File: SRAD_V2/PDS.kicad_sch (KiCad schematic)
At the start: 16 parts, among them IC7 TPS563200, J5 Conn_01x02_Pin

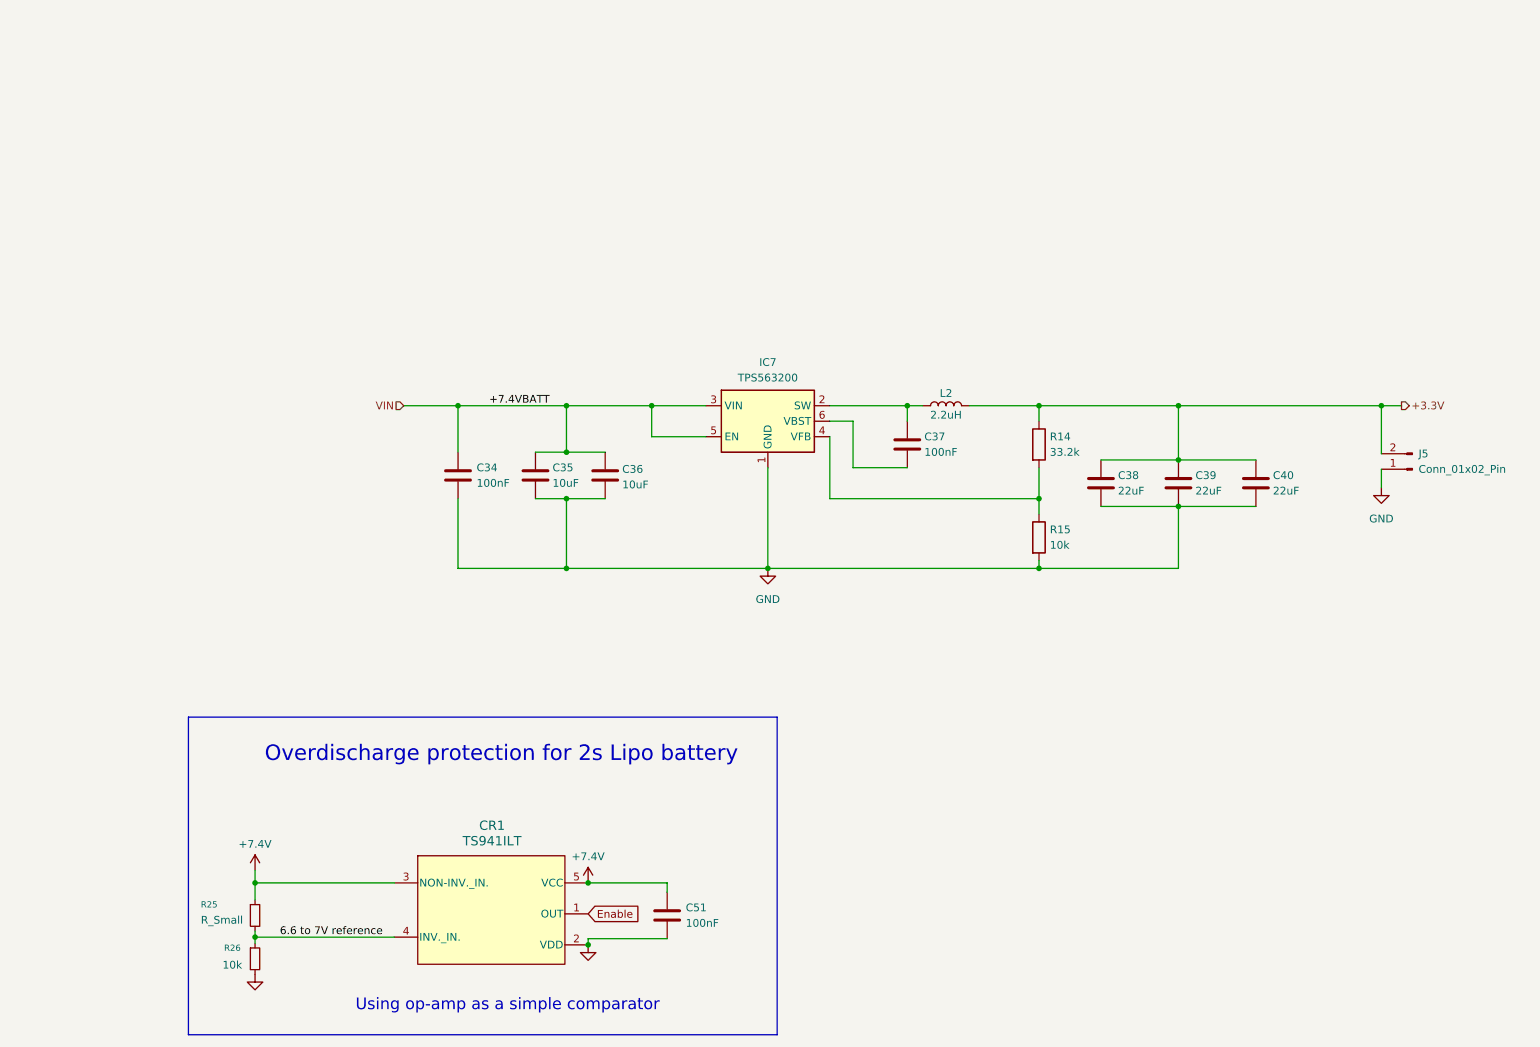
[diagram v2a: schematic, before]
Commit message: Added component descriptions for BOM and added logos on silkscreen
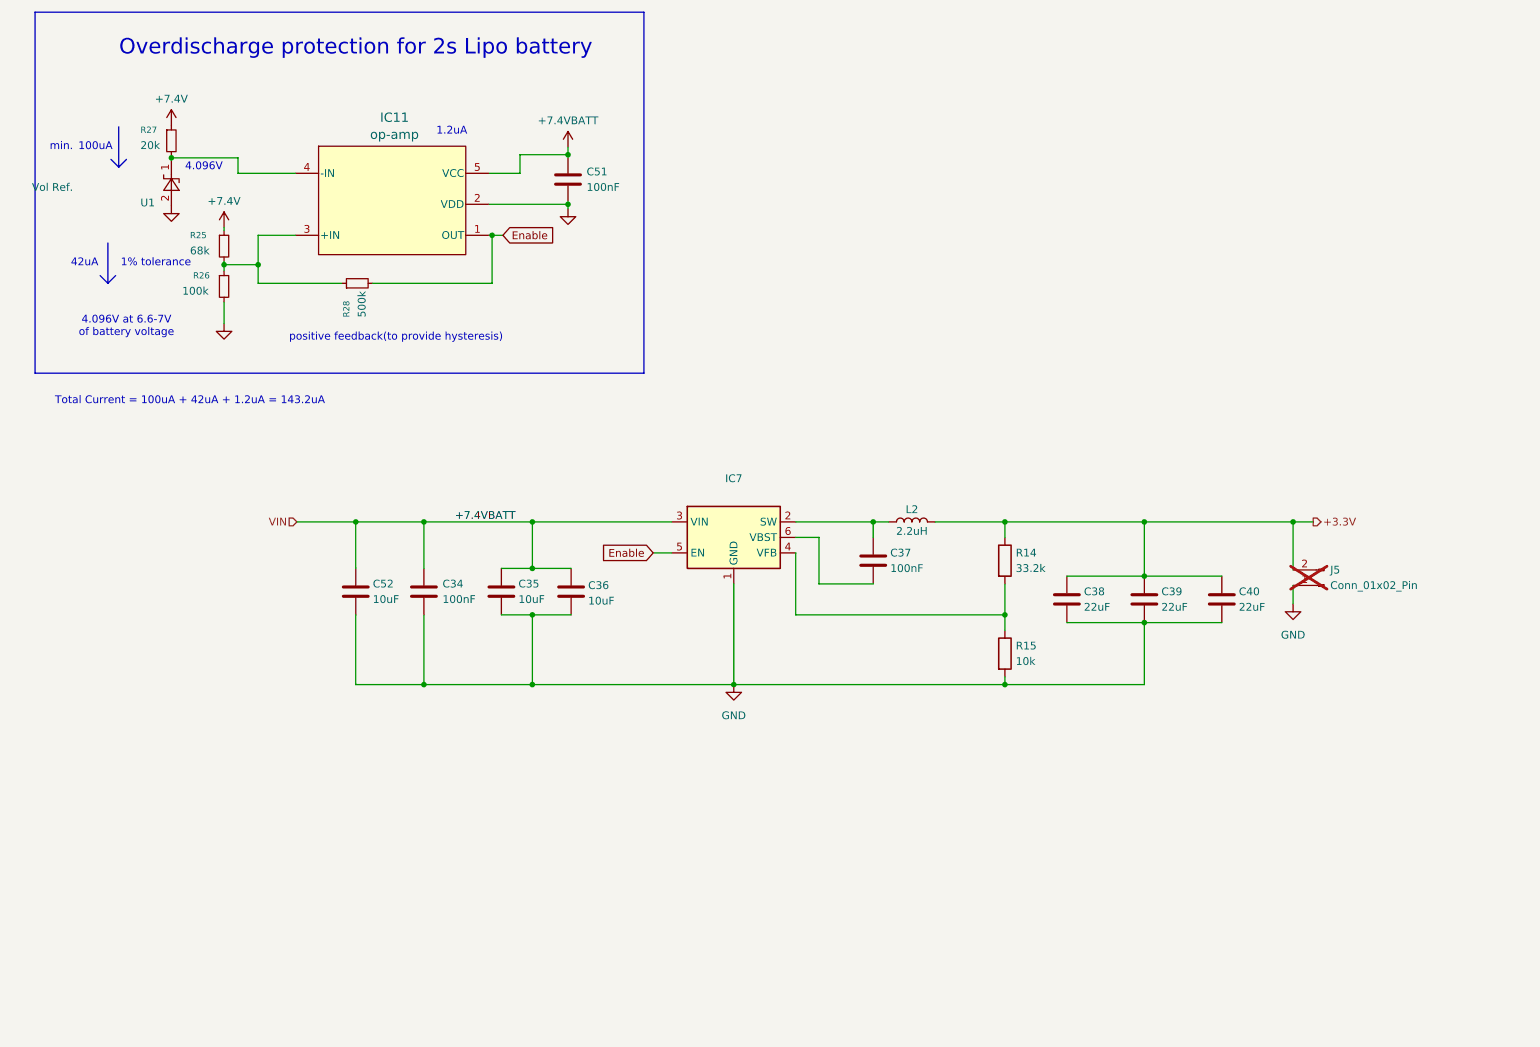
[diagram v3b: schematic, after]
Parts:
- added C52: 10uF, Capacitor_SMD:C_1206_3216Metric, symbol Device:C
- added R27: 20k, Resistor_SMD:R_0603_1608Metric, symbol Device:R_Small
- added R28: 500k, Resistor_SMD:R_0603_1608Metric, symbol Device:R_Small
- added U1: Vol Ref., Package_TO_SOT_SMD:SOT-23, symbol Reference_Voltage:LM4040DBZ-2.0
- C34, C37, C51: Digikey Link (none) -> https://www.digikey.ca/en/products/detail/kemet/C0603C104K5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; Manufacturer_Name (none) -> KEMET; Manufacturer_Part_Number (none) -> C0603C104K5RAC3121
- C35, C36: Digikey Link (none) -> https://www.digikey.com/en/products/detail/tdk/CGA5L1X7R1E1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; Manufacturer_Name (none) -> TDK; Manufacturer_Part_Number (none) -> CGA5L1X7R1E106K160DC
- C38, C39, C40: Digikey Link (none) -> https://www.digikey.com/en/products/detail/murata-electroni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; Manufacturer_Name (none) -> Murata Electronics; Manufacturer_Part_Number (none) -> GRM31CC81E226ME11L
- IC11: renamed from CR1; value TS941ILT -> op-amp; footprint TS941ILT:SOT23-5L_STM -> SOT23-5L_STM; Digikey Link (none) -> https://www.digikey.ca/en/products/detail/stmicroelectronic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; Manufacturer_Name (none) -> STMicroelectronics; Manufacturer_Part_Number (none) -> TS941ILT
- IC7: value TPS563200 -> (none); Digikey Link (none) -> https://www.digikey.ca/en/products/detail/texas-instruments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; Manufacturer_Name (none) -> Texas Instruments; Manufacturer_Part_Number (none) -> TPS563200DDCT
- J5: now not fitted
- L2: Digikey Link (none) -> https://www.digikey.ca/en/products/detail/bourns-inc/srp503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; Manufacturer_Name (none) -> Bourns Inc.; Manufacturer_Part_Number (none) -> SRP5030TA-2R2M
- R14: Digikey Link (none) -> https://www.digikey.ca/en/products/detail/vishay-dale/crcw0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; Manufacturer_Name (none) -> Vishay Dale; Manufacturer_Part_Number (none) -> CRCW060333K2FKTA
- R15: Digikey Link (none) -> https://www.digikey.ca/en/products/detail/bourns-inc/crt060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; Manufacturer_Name (none) -> Bourns Inc.; Manufacturer_Part_Number (none) -> CRT0603-BY-1002ELF
- R25: value R_Small -> 68k; Digikey Link (none) -> https://www.digikey.ca/en/products/detail/te-connectivity-p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; Manufacturer_Name (none) -> TE Connectivity Passive Product; Manufacturer_Part_Number (none) -> CRG0603F68K
- R26: value 10k -> 100k; Digikey Link (none) -> https://www.digikey.ca/en/products/detail/yageo/rt0603frd07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; Manufacturer_Name (none) -> YAGEO; Manufacturer_Part_Number (none) -> RT0603FRD07100KL
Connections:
- net +7.4V: now also R27.1; no longer C51.1, IC11.3 (NON-INV._IN.), IC11.5 (VCC)
- net Enable: now also IC7.5 (EN), R28.2
- net GND: now also C52.2, U1.2 (A)
- net 6.6 to 7V reference: no longer names the net of R25.2, R26.1
- net 6.6 to 7V reference: now also IC11.3 (+IN), R28.1; no longer IC11.4 (INV._IN.)
- net VIN renamed +7.4VBATT
- net +7.4VBATT: now also C51.1, IC11.5 (VCC), C52.1; no longer IC7.5 (EN)
- new net: IC11.4 (-IN), R27.2, U1.1 (K)
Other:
- note added: "1% tolerance"
- note added: "1.2uA"
- note added: "100uA"
- note added: "4.096V"
- note added: "4.096V at 6.6-7V of battery voltage"
- note added: "42uA"
- note added: "Total Current = 100uA + 42uA + 1.2uA = 143.2uA"
- note added: "min."
- note added: "positive feedback(to provide hysteresis)"
- note removed: "Using op-amp as a simple comparator"
- moved on the sheet: C34, C35, C36, C37, C38, C39, C40, C51, IC11, IC7, L2, R14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

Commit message: Updated the 3.3V test point
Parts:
- removed J5: Conn_01x02_Pin, Connector_PinHeader_1.27mm:PinHeader_1x02_P1.27mm_Vertical, symbol Connector:Conn_01x02_Pin
- added J5: Conn_01x01_Pin, Connector_PinHeader_1.27mm:PinHeader_1x01_P1.27mm_Vertical, symbol Connector:Conn_01x01_Pin
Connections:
- net +3.3V: now also J5.1 (Pin_1)
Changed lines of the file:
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@@
 	(wire
 		(pts
-			(xy 223.266 110.744) (xy 223.266 113.792)
-		)
-		(stroke
-			(width 0)
-			(type default)
-		)
-	)
-	(wire
-		(pts
 			(xy 80.772 115.57) (xy 80.772 127)
 		)
@@
 	(wire
 		(pts
-			(xy 223.266 100.33) (xy 223.266 108.204)
+			(xy 223.266 100.33) (xy 223.266 109.22)
 		)
 		(stroke
@@
 	(wire
 		(pts
+			(xy 227.838 109.22) (xy 223.266 109.22)
+		)
+		(stroke
+			(width 0)
+			(type default)
+		)
+	)
+	(wire
+		(pts
 			(xy 223.266 100.33) (xy 226.568 100.33)
 		)
@@
 	)
 	(symbol
-		(lib_id "power:+BATT")
-		(at 48.006 52.07 0)
+		(lib_id "Connector:Conn_01x01_Pin")
+		(at 232.918 109.22 180)
 		(unit 1)
 		(body_style 1)
 		(exclude_from_sim no)
-		(in_bom yes)
+		(in_bom no)
 		(on_board yes)
-		(in_pos_files yes)
-		(dnp no)
-		(property "Reference" "#PWR076"
-			(at 48.006 55.88 0)
-			(hide yes)
+		(in_pos_files no)
+		(dnp yes)
+		(fields_autoplaced yes)
+		(property "Reference" "J5"
+			(at 232.283 103.886 0)
 			(show_name no)
 			(do_not_autoplace no)
@@
 			)
 		)
-		(property "Value" "+7.4V"
-			(at 48.006 47.752 0)
+		(property "Value" "Conn_01x01_Pin"
+			(at 232.283 106.426 0)
 			(show_name no)
 			(do_not_autoplace no)
@@
 			)
 		)
-		(property "Footprint" ""
-			(at 48.006 52.07 0)
+		(property "Footprint" "Connector_PinHeader_1.27mm:PinHeader_1x01_P1.27mm_Vertical"
+			(at 232.918 109.22 0)
 			(hide yes)
 			(show_name no)
@@
 		)
 		(property "Datasheet" ""
-			(at 48.006 52.07 0)
+			(at 232.918 109.22 0)
 			(hide yes)
 			(show_name no)
@@
 			)
 		)
-		(property "Description" "Power symbol creates a global label with name \"+BATT\""
-			(at 48.006 52.07 0)
+		(property "Description" "Generic connector, single row, 01x01, script generated"
+			(at 232.918 109.22 0)
 			(hide yes)
 			(show_name no)
@@
 			(project "SRAD_V2"
 				(path "/016ea6e5-09c6-43d4-b6cc-3404e2d65458/9c8bbba4-8714-49e8-941c-914b77648ac5"
-					(reference "#PWR076")
+					(reference "J5")
 					(unit 1)
 				)
@@
 	)
 	(symbol
-		(lib_id "power:GND")
-		(at 223.266 113.792 0)
+		(lib_id "power:+BATT")
+		(at 48.006 52.07 0)
 		(unit 1)
 		(body_style 1)
@@
 		(in_pos_files yes)
 		(dnp no)
-		(fields_autoplaced yes)
-		(property "Reference" "#PWR047"
-			(at 223.266 120.142 0)
+		(property "Reference" "#PWR076"
+			(at 48.006 55.88 0)
 			(hide yes)
 			(show_name no)
@@
 			)
 		)
-		(property "Value" "GND"
-			(at 223.266 118.872 0)
+		(property "Value" "+7.4V"
+			(at 48.006 47.752 0)
 			(show_name no)
 			(do_not_autoplace no)
@@
 		)
 		(property "Footprint" ""
-			(at 223.266 113.792 0)
+			(at 48.006 52.07 0)
 			(hide yes)
 			(show_name no)
@@
 		)
 		(property "Datasheet" ""
-			(at 223.266 113.792 0)
+			(at 48.006 52.07 0)
 			(hide yes)
 			(show_name no)
@@
 			)
 		)
-		(property "Description" "Power symbol creates a global label with name \"GND\" , ground"
-			(at 223.266 113.792 0)
+		(property "Description" "Power symbol creates a global label with name \"+BATT\""
+			(at 48.006 52.07 0)
 			(hide yes)
 			(show_name no)
@@
 			(project "SRAD_V2"
 				(path "/016ea6e5-09c6-43d4-b6cc-3404e2d65458/9c8bbba4-8714-49e8-941c-914b77648ac5"
-					(reference "#PWR047")
+					(reference "#PWR076")
 					(unit 1)
 				)
@@
 					(unit 1)
 				)
-			)
-		)
-	)
-	(symbol
-		(lib_id "Connector:Conn_01x02_Pin")
-		(at 228.346 110.744 180)
-		(unit 1)
-		(body_style 1)
-		(exclude_from_sim no)
-		(in_bom yes)
-		(on_board yes)
-		(in_pos_files no)
-		(dnp yes)
-		(fields_autoplaced yes)
-		(property "Reference" "J5"
-			(at 229.362 108.2039 0)
-			(show_name no)
-			(do_not_autoplace no)
-			(effects
-				(font
-					(size 1.27 1.27)
-				)
-				(justify right)
-			)
-		)
-		(property "Value" "Conn_01x02_Pin"
-			(at 229.362 110.7439 0)
-			(show_name no)
-			(do_not_autoplace no)
-			(effects
-				(font
-					(size 1.27 1.27)
-				)
-				(justify right)
-			)
-		)
-		(property "Footprint" "Connector_PinHeader_1.27mm:PinHeader_1x02_P1.27mm_Vertical"
-			(at 228.346 110.744 0)
-			(hide yes)
-			(show_name no)
-			(do_not_autoplace no)
-			(effects
-				(font
-					(size 1.27 1.27)
-				)
-			)
-		)
-		(property "Datasheet" ""
-			(at 228.346 110.744 0)
-			(hide yes)
-			(show_name no)
-			(do_not_autoplace no)
-			(effects
-				(font
-					(size 1.27 1.27)
-				)
-			)
-		)
-		(property "Description" "Generic connector, single row, 01x02, script generated"
-			(at 228.346 110.744 0)
-			(hide yes)
-			(show_name no)
-			(do_not_autoplace no)
-			(effects
-				(font
-					(size 1.27 1.27)
-				)
-			)
-		)
-		(property "Digikey Link" ""
-			(at 228.346 110.744 0)
-			(hide yes)
-			(show_name no)
-			(do_not_autoplace no)
-			(effects
-				(font
-					(size 1.27 1.27)
-				)
-			)
-		)
-		(pin "1"
-		)
-		(pin "2"
-		)
-		(instances
-			(project "SRAD_V2"
-				(path "/016ea6e5-09c6-43d4-b6cc-3404e2d65458/9c8bbba4-8714-49e8-941c-914b77648ac5"
-					(reference "J5")
-					(unit 1)
-				)
